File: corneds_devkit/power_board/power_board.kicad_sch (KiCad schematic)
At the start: 0 parts

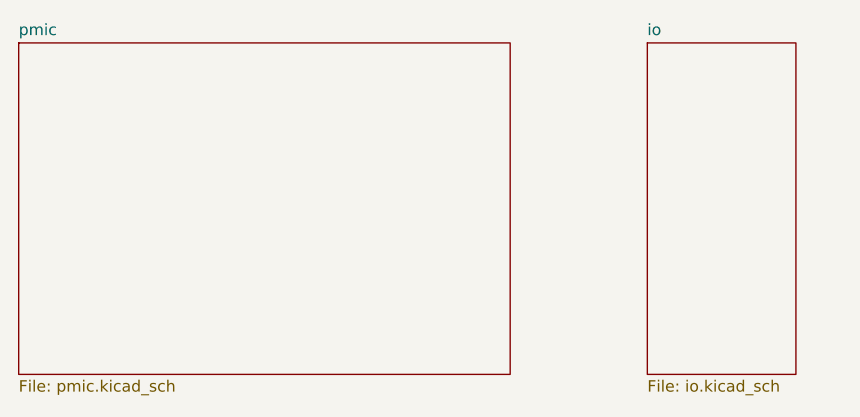
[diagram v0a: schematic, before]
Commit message: made power schematic and started on routing power board
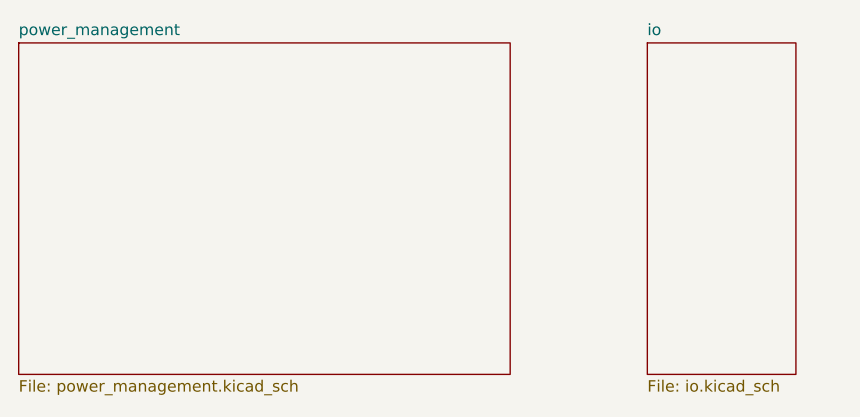
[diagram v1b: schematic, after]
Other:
- sheet pmic renamed power_management
- sheet power_management: file pmic.kicad_sch -> power_management.kicad_sch
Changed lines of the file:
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@@
 			(color 0 0 0 0.0000)
 		)
-		(property "Sheetname" "pmic"
+		(property "Sheetname" "power_management"
 			(at 39.37 32.3084 0)
 			(effects
@@
 			)
 		)
-		(property "Sheetfile" "pmic.kicad_sch"
+		(property "Sheetfile" "power_management.kicad_sch"
 			(at 39.37 70.4346 0)
 			(effects
